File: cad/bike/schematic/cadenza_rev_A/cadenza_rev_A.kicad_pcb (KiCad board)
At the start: 2 copper layers, 80 x 50 mm, 35 parts, among them J2 USB_C_Receptacle, J3 Conn_01x02, Q1 BC547, U1 TLC5916, U10 HDSP-A151, U11 TLC5916, U12 HDSP-A151, U13 STM32F105RCTx, U14 INA193, U15 TLC5916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

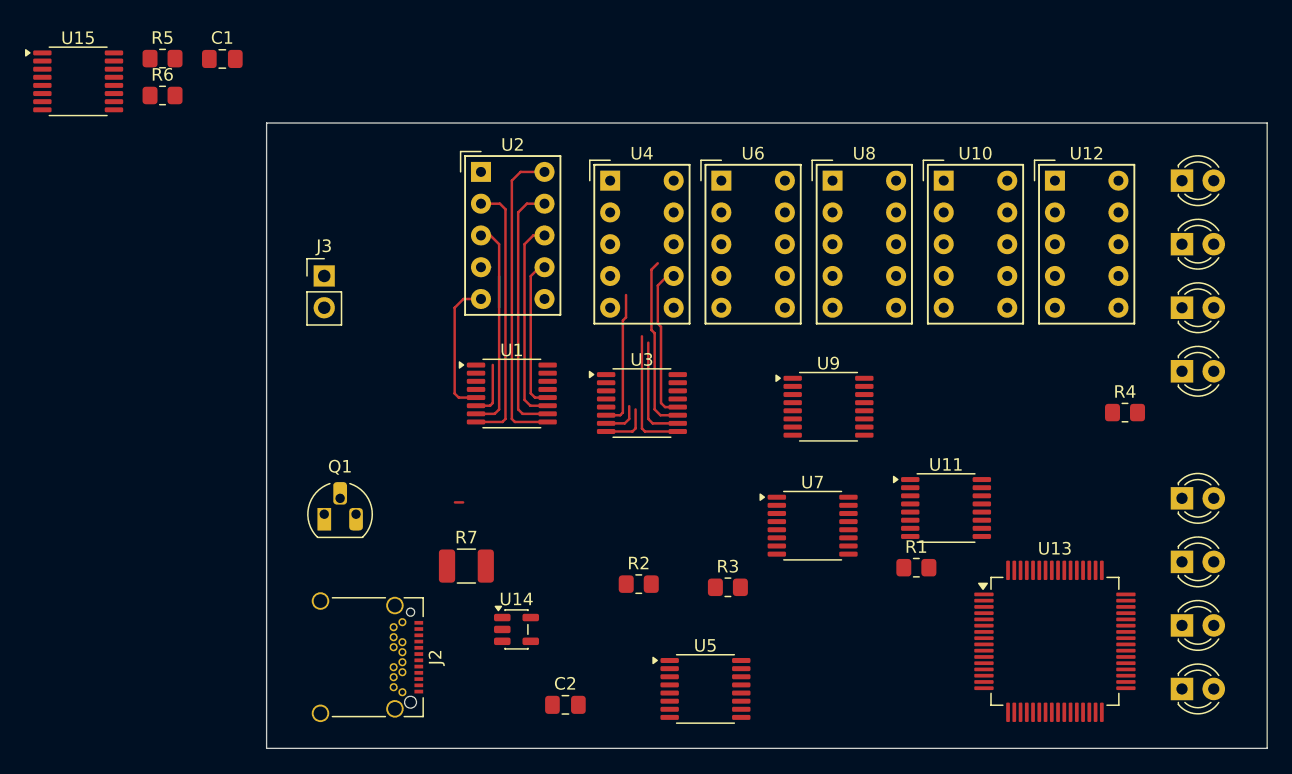
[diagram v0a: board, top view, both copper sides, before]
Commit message: rearranged parts placement
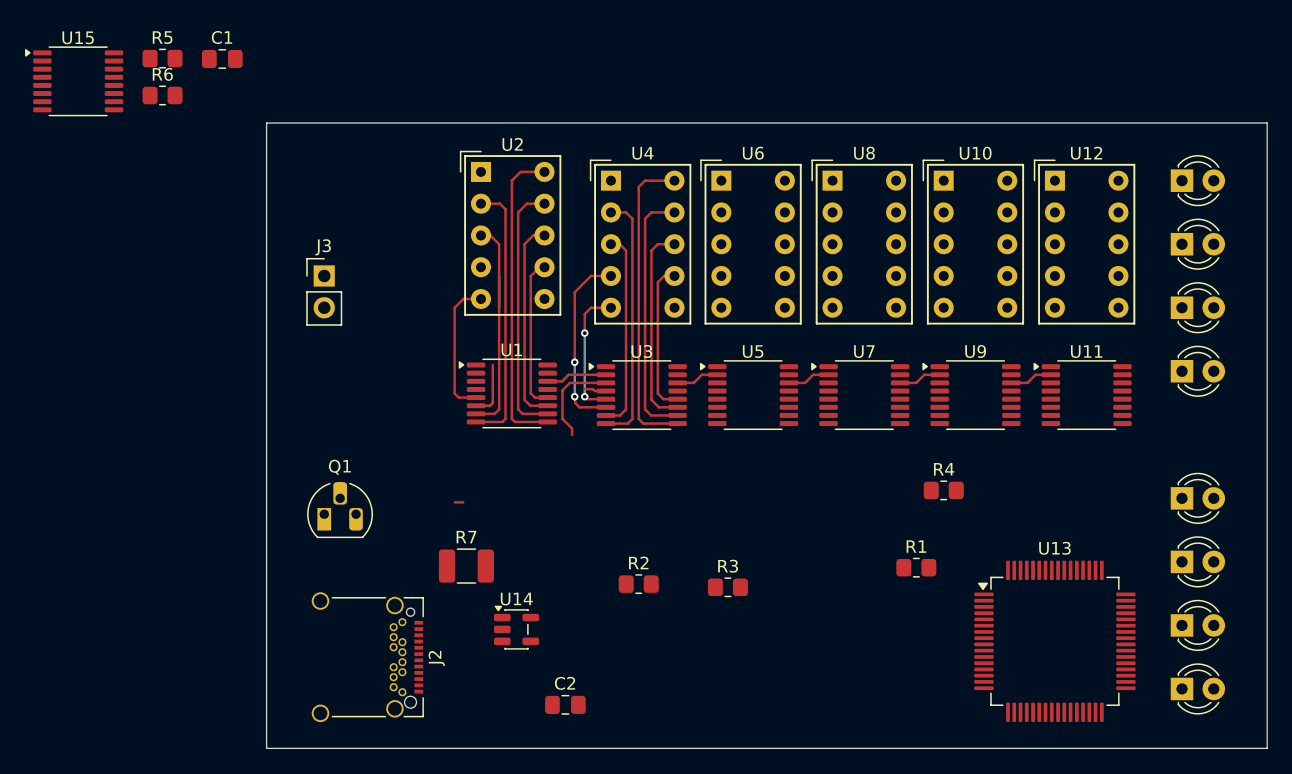
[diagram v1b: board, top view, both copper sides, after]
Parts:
- moved U5 23.8 mm to (88.9, 71.8)
- moved R4 15.8 mm to (104.1, 79.4)
- moved U11 14.4 mm to (115.6, 71.8)
- moved U9 11.8 mm to (106.7, 71.8)
- moved U7 11.2 mm to (97.8, 71.8)
- moved U3 0.64 mm to (80.0, 71.8)
- moved U4 0.06 mm to (77.5, 54.6)
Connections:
- U3 pad 10: unconnected-(U3-~{OUT5}-Pad10) -> Net-(U3-~{OUT5})
- U3 pad 11: unconnected-(U3-~{OUT6}-Pad11) -> Net-(U3-~{OUT6})
- U3 pad 5: unconnected-(U3-~{OUT0}-Pad5) -> Net-(U3-~{OUT0})
- U3 pad 6: unconnected-(U3-~{OUT1}-Pad6) -> Net-(U3-~{OUT1})
- U3 pad 7: unconnected-(U3-~{OUT2}-Pad7) -> Net-(U3-~{OUT2})
- U3 pad 8: unconnected-(U3-~{OUT3}-Pad8) -> Net-(U3-~{OUT3})
- U3 pad 9: unconnected-(U3-~{OUT4}-Pad9) -> Net-(U3-~{OUT4})
- U4 pad 10: unconnected-(U4-A-Pad10) -> Net-(U3-~{OUT4})
- U4 pad 2: unconnected-(U4-F-Pad2) -> Net-(U3-~{OUT3})
- U4 pad 3: unconnected-(U4-G-Pad3) -> Net-(U3-~{OUT2})
- U4 pad 4: unconnected-(U4-E-Pad4) -> Net-(U3-~{OUT1})
- U4 pad 5: unconnected-(U4-D-Pad5) -> Net-(U3-~{OUT0})
- U4 pad 8: unconnected-(U4-C-Pad8) -> Net-(U3-~{OUT6})
- U4 pad 9: unconnected-(U4-B-Pad9) -> Net-(U3-~{OUT5})
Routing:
- net Net-(U3-~{OUT4}): track 0.00 -> 24.9 mm
- net Net-(U3-~{OUT5}): track 0.00 -> 20.6 mm
- net Net-(U3-~{OUT3}): track 0.00 -> 20.2 mm
- net Net-(U3-~{OUT6}): track 0.00 -> 16.3 mm
- net Net-(U3-~{OUT2}): track 0.00 -> 15.9 mm
- net Net-(U3-~{OUT1}): track 0.00 -> 15.0 mm, vias 0 -> 2
- net unconnected-(U3-~{OUT6}-Pad11): track 14.0 -> 0.00 mm
- net unconnected-(U3-~{OUT1}-Pad6): track 10.9 -> 0.00 mm
- net Net-(U3-~{OUT0}): track 0.00 -> 10.7 mm, vias 0 -> 2
- net unconnected-(U3-~{OUT4}-Pad9): track 10.3 -> 0.00 mm
- net unconnected-(U3-~{OUT5}-Pad10): track 8.60 -> 0.00 mm
- net Net-(U1-CLK): track 0.00 -> 7.60 mm
- net Net-(U1-SDO): track 0.00 -> 4.88 mm
- net unconnected-(U3-~{OUT3}-Pad8): track 3.98 -> 0.00 mm
- net Net-(U3-SDO): track 0.00 -> 3.44 mm
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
